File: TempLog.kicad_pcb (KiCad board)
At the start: 2 copper layers, 57 x 54.5 mm, 50 parts, among them J1 1.27, 2x5, Male, TH, J2 Conn_01x02, J3 Conn_01x03, J5 Conn_01x02, J6 USB4105-GF-A-060, Q1 DMP6350S, SW1 SMD_4.6x2.8mm_h1.9mm, SW2 SMD_4.6x2.8mm_h1.9mm, U1 STM32F030C8Tx, U2 GD25Q16CSJGR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

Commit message: updated library links
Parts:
- removed J2: Conn_01x02, Connector_PinHeader_2.54mm:PinHeader_1x02_P2.54mm_Vertical
- removed Q1: DMP6350S, SparkFun-Semiconductor-Standard:SOT23-3
- removed R1, R2: 49.9K, Resistor_SMD:R_0805_2012Metric
- removed R3: 150K, Resistor_SMD:R_0805_2012Metric
- removed R4, R5: 10M, Resistor_SMD:R_0805_2012Metric
- removed TP1, TP3, TP4: TestPoint, TestPoint:TestPoint_Pad_D1.0mm
- removed U4: LM321, Package_TO_SOT_SMD:SOT-23-5
- added J7: Conn_01x02, Connector_PinHeader_2.54mm:PinHeader_1x02_P2.54mm_Vertical, F.Cu at (185.1, 103.9)
- added R12: 5K, Resistor_SMD:R_0805_2012Metric, F.Cu at (189.6, 103.0)
- added R13: 5K, Resistor_SMD:R_0805_2012Metric, F.Cu at (189.6, 106.0)
- C2, C3: value 1.0uF -> 100nF
- SW1, SW2: footprint SparkFun-Switch:Push_SMD_4.6x2.8mm -> SparkFun-Switch:Push_SMD_4.6x2.8mm_h1.9mm
- U2: value GD25Q16CSJGR -> GD25Q16CSJGR
- U3: value LM321 -> TMP1075DGK; footprint Package_TO_SOT_SMD:SOT-23-5 -> Package_SO:VSSOP-8_3x3mm_P0.65mm
- Y1: footprint Crystal:Crystal_SMD_5032-2Pin_5.0x3.2mm -> SparkFun-Clock:Crystal_SMD_3.2x1.5mm
- Y2: footprint Crystal:Crystal_SMD_MicroCrystal_CC7V-T1A-2Pin_3.2x1.5mm -> SparkFun-Clock:Crystal_SMD_3.2x1.5mm
- moved U3 60.5 mm to (193.5, 91.5)
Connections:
- J6 pad VBUS: VCC -> Net-(J7-Pin_1)
- U1 pad 19: TEMP_EN -> unconnected-(U1-PB1-Pad19)
- U1 pad 20: THERM_OUT -> unconnected-(U1-PB2-Pad20)
- U1 pad 21: THERM_OFST -> SCL
- U1 pad 22: unconnected-(U1-PB11-Pad22) -> SDA
- U3 pad 1: Net-(J2-Pin_1) -> SDA
- U3 pad 2: GND -> SCL
- U3 pad 3: THERM_OUT -> GND
- U3 pad 4: THERM_OUT -> GND
- U3 pad 5: TEMP_EN -> GND
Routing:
- net unconnected-(U1-PB1-Pad19): track 0.00 -> 63.5 mm, vias 0 -> 5
- net TEMP_EN: track 63.5 -> 0.00 mm, vias 5 -> 0
- net (no net): track 0.00 -> 29.1 mm, vias 0 -> 2
- net THERM_OFST: track 28.2 -> 0.00 mm
- net SCL: track 0.00 -> 28.2 mm
- net unconnected-(U1-PB2-Pad20): track 0.00 -> 27.0 mm, vias 0 -> 2
- net THERM_OUT: track 27.0 -> 0.00 mm, vias 2 -> 0
- net Net-(Q1-D): track 12.3 -> 0.00 mm, vias 2 -> 0
- net Net-(J2-Pin_2): track 8.09 -> 0.00 mm
- net SDA: track 0.00 -> 7.38 mm
- net Net-(J2-Pin_1): track 7.38 -> 0.00 mm
- net Net-(Q1-G): track 5.60 -> 0.00 mm
- net Net-(Q1-S): track 3.14 -> 0.00 mm

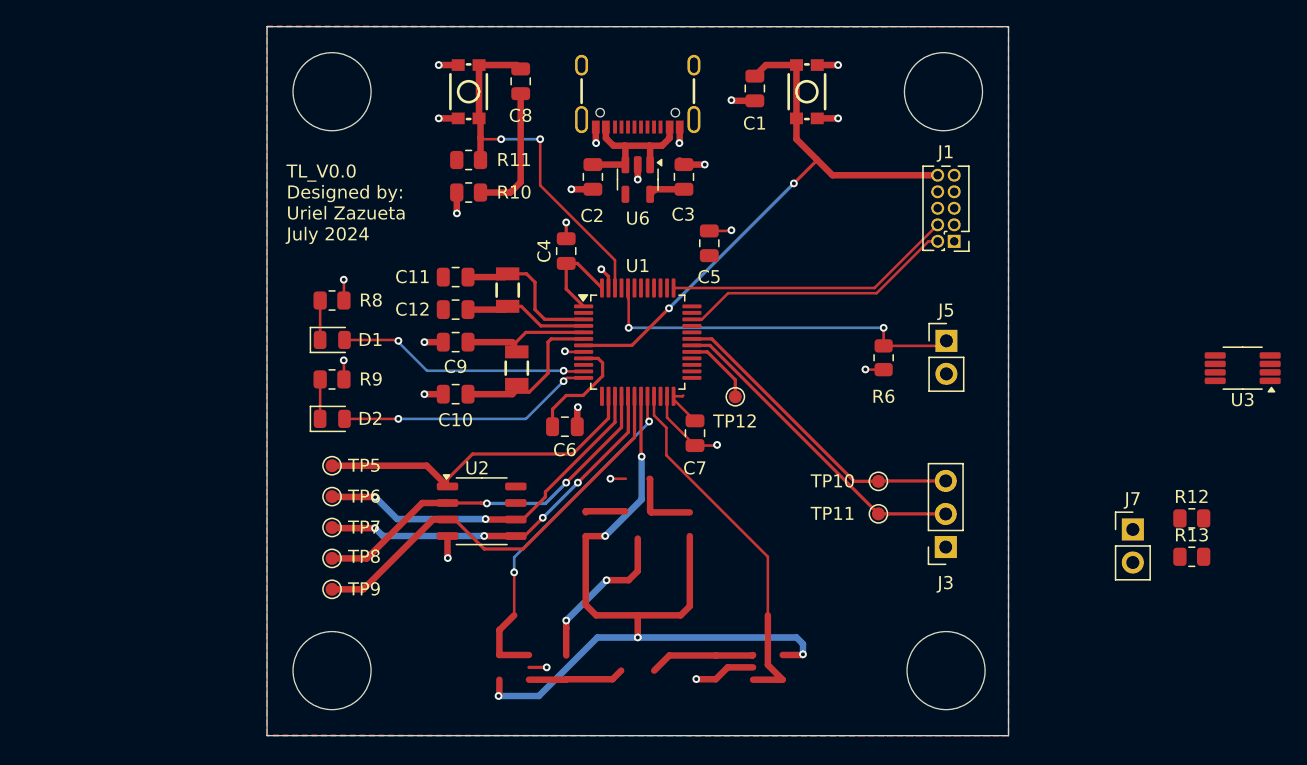
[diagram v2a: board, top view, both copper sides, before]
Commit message: Changed board size to 50mm x 40mm and rerouted the nets
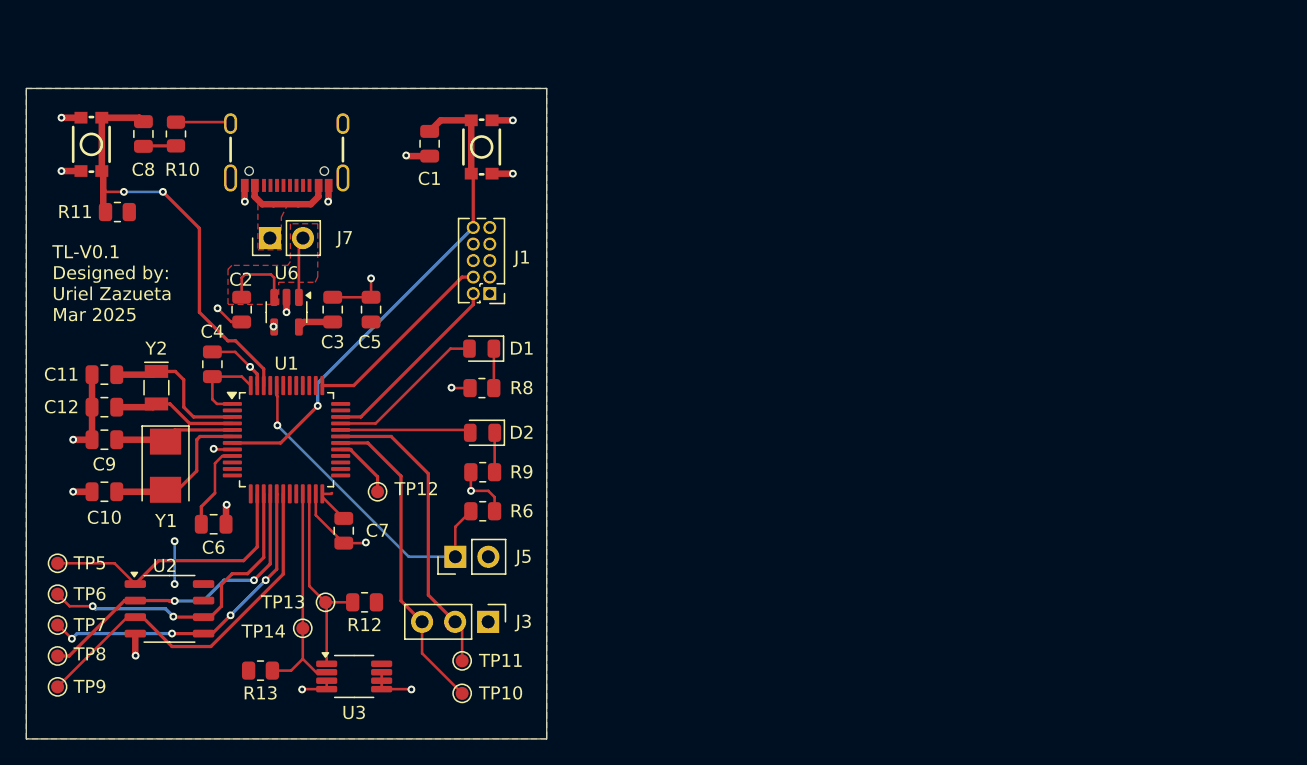
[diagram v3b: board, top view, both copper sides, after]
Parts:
- added TP13: TestPoint, TestPoint:TestPoint_Pad_D1.0mm, F.Cu at (123.0, 109.5)
- added TP14: TestPoint, TestPoint:TestPoint_Pad_D1.0mm, F.Cu at (121.2, 111.5)
- J3: footprint Connector_PinSocket_2.54mm:PinSocket_1x03_P2.54mm_Vertical -> Connector_PinHeader_2.54mm:PinHeader_1x03_P2.54mm_Vertical
- R12, R13: value 5K -> 10K
- Y1: footprint SparkFun-Clock:Crystal_SMD_3.2x1.5mm -> Crystal:Crystal_SMD_5032-2Pin_5.0x3.2mm
- Y2: footprint SparkFun-Clock:Crystal_SMD_3.2x1.5mm -> Crystal:Crystal_SMD_MicroCrystal_CC7V-T1A-2Pin_3.2x1.5mm
- moved U3 72.3 mm to (125.2, 115.2), turned to 0 degrees
- moved R13 72.1 mm to (118.0, 114.8)
- moved J7 70.0 mm to (118.7, 81.5), turned to 90 degrees
- moved R12 63.9 mm to (126.0, 109.5), turned to 180 degrees
- moved J5 41.2 mm to (133.0, 106.0), turned to 90 degrees
- moved J1 35.9 mm to (135.6, 85.8)
- moved TP10 35.9 mm to (133.5, 116.5)
- moved J3 35.6 mm to (135.5, 111.0), turned to -90 degrees
- moved TP11 33.9 mm to (133.5, 114.0)
- moved R6 33.0 mm to (135.1, 102.5), turned to 180 degrees
- moved C8 29.3 mm to (109.0, 73.5)
- moved SW2 29.3 mm to (105.0, 74.3)
- moved C2 28.9 mm to (116.5, 87.0)
- moved C3 28.9 mm to (123.5, 87.0)
- moved U6 28.9 mm to (120.0, 87.2)
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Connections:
- net Net-(J7-Pin_1) renamed VBUS
- J3 pad 2: USART1_TX -> USART1_RX
- J3 pad 3: USART1_RX -> USART1_TX
- TP10 pad 1: USART1_RX -> USART1_TX
- TP11 pad 1: USART1_TX -> USART1_RX
- U1 pad 11: LED0 -> unconnected-(U1-PA1-Pad11)
- U1 pad 12: LED1 -> unconnected-(U1-PA2-Pad12)
- U1 pad 32: unconnected-(U1-PA11-Pad32) -> LED1
- U1 pad 33: unconnected-(U1-PA12-Pad33) -> LED0
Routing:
- net unconnected-(U1-PB1-Pad19): track 63.5 -> 0.00 mm, vias 5 -> 0
- net (no net): track 29.1 -> 0.00 mm, vias 2 -> 0
- net unconnected-(U1-PB2-Pad20): track 27.0 -> 0.00 mm, vias 2 -> 0
- net GND: track 47.4 -> 58.7 mm, vias 26 -> 21
- net SCL: track 28.2 -> 17.7 mm
- net LED1: track 19.7 -> 10.1 mm, vias 2 -> 0
- net SDA: track 7.38 -> 15.7 mm
- net Net-(C8-Pad2): track 10.2 -> 2.52 mm
- net SWDCLK: track 22.3 -> 15.1 mm
- net VBUS: track 0.00 -> 7.08 mm
- net LED0: track 19.3 -> 12.3 mm, vias 2 -> 0
- net NRST: track 45.1 -> 38.3 mm, vias 2 -> 1
- net SWDIO: track 21.4 -> 14.6 mm
- net BTN_1: track 29.1 -> 33.7 mm
- net FLASH_nCS: track 25.6 -> 21.3 mm
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- added copper zone on F.Cu, net VBUS
- added copper zone on F.Cu, net VCC
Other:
- board size 57 x 54.5 mm -> 40 x 50 mm
- board text added: "TL-V0.1 Designed by: Uriel Zazueta Mar 2025"
- board text removed: "TL_V0.0 Designed by: Uriel Zazueta July 2024"
